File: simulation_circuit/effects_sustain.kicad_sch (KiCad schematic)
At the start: 14 parts, among them Q1 BC547

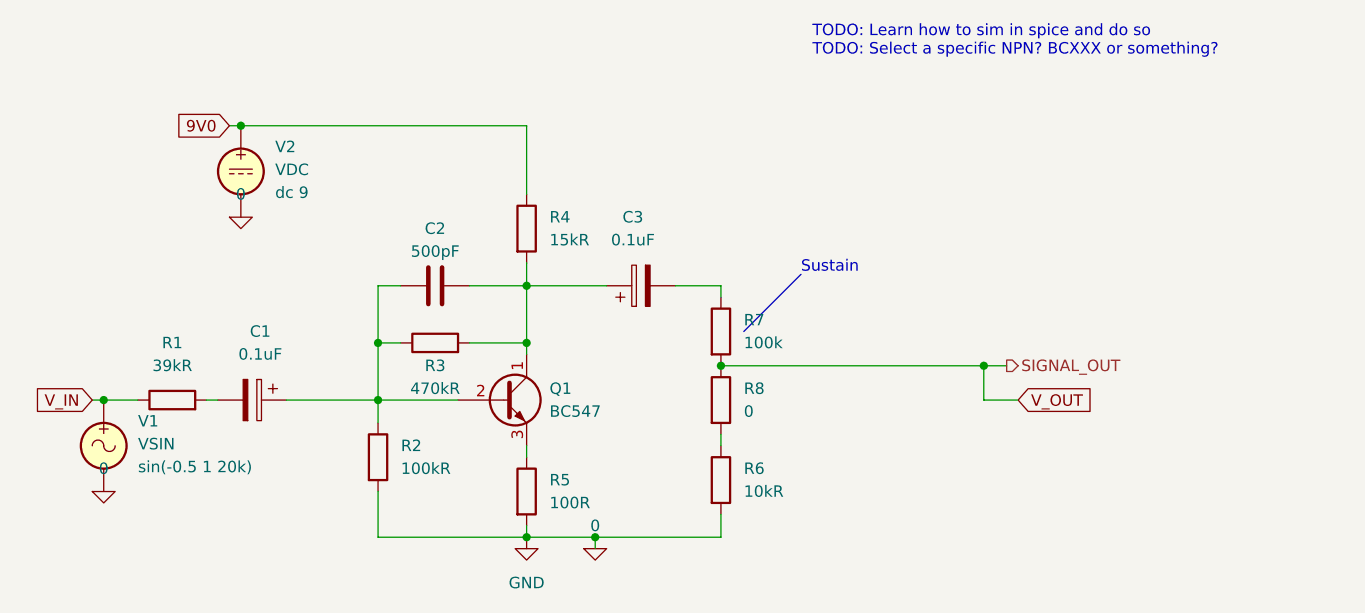
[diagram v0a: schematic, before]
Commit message: added decoupling cap and series resistor to output side of sustain effect, added subfolder to contain simulation results to put in design notes. Added simulation results for sustain effect to design notes
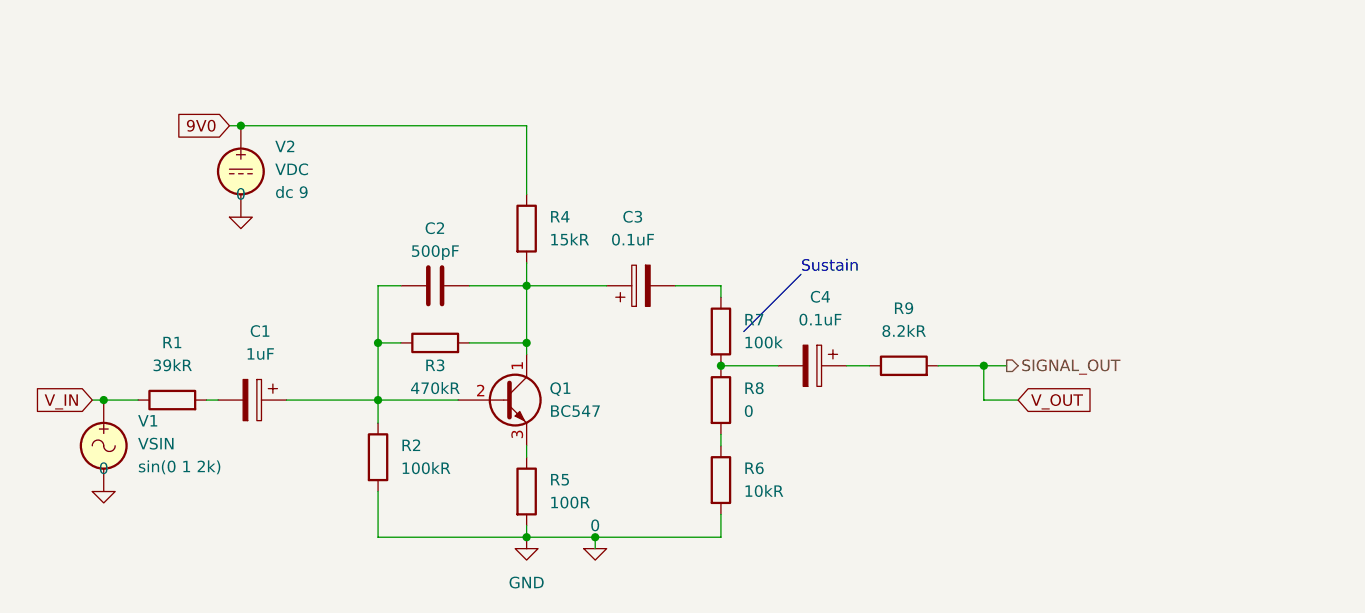
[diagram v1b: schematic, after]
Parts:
- added C4: 0.1uF, symbol Device:C_Polarized
- added R9: 8.2kR, symbol Device:R
- C1: value 0.1uF -> 1uF
- Q1: Spice_Lib_File /home/liam/Documents/big_muff_pi_copy/SPICE_MODELS.lib -> /home/liam/big_muff_pi_copy/SPICE_MODELS.lib
- V1: Spice_Model sin(-0.5 1 20k) -> sin(0 1 2k)
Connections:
- net V_OUT: now also R9.2; no longer R7.2, R8.1
- new net: C4.2, R7.2, R8.1
- new net: C4.1, R9.1
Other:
- note removed: "TODO: Learn how to sim in spice and do so TODO: Select a specific NPN? BCXXX or something?"
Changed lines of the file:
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@@
 (kicad_sch (version 20211123) (generator eeschema)
   (paper "A4")
+  (junction (at 148.59 109.22) (diameter 0) (color 0 0 0 0)
+  )
+  (junction (at 148.59 81.28) (diameter 0) (color 0 0 0 0)
+  )
+  (junction (at 116.84 63.5) (diameter 0) (color 0 0 0 0)
+  )
   (junction (at 170.18 90.17) (diameter 0) (color 0 0 0 0)
   )
-  (junction (at 148.59 109.22) (diameter 0) (color 0 0 0 0)
-  )
-  (junction (at 148.59 81.28) (diameter 0) (color 0 0 0 0)
-  )
-  (junction (at 116.84 63.5) (diameter 0) (color 0 0 0 0)
-  )
   (junction (at 132.08 93.98) (diameter 0) (color 0 0 0 0)
   )
@@
   )
   (wire (pts (xy 132.08 93.98) (xy 140.97 93.98))
-    (stroke (width 0) (type default) (color 0 0 0 0))
-  )
-  (wire (pts (xy 170.18 90.17) (xy 199.39 90.17))
     (stroke (width 0) (type default) (color 0 0 0 0))
   )
@@
     (stroke (width 0) (type default) (color 0 0 0 0))
   )
+  (wire (pts (xy 194.31 90.17) (xy 199.39 90.17))
+    (stroke (width 0) (type default) (color 0 0 0 0))
+  )
   (wire (pts (xy 148.59 107.95) (xy 148.59 109.22))
     (stroke (width 0) (type default) (color 0 0 0 0))
@@
     (stroke (width 0) (type default) (color 0 0 0 0))
   )
+  (wire (pts (xy 170.18 90.17) (xy 176.53 90.17))
+    (stroke (width 0) (type default) (color 0 0 0 0))
+  )
   (wire (pts (xy 199.39 90.17) (xy 201.93 90.17))
     (stroke (width 0) (type default) (color 0 0 0 0))
@@
     (stroke (width 0) (type default) (color 0 0 0 0))
   )
+  (wire (pts (xy 184.15 90.17) (xy 186.69 90.17))
+    (stroke (width 0) (type default) (color 0 0 0 0))
+  )
   (wire (pts (xy 148.59 78.74) (xy 148.59 81.28))
     (stroke (width 0) (type default) (color 0 0 0 0))
@@
   (wire (pts (xy 170.18 97.79) (xy 170.18 99.06))
     (stroke (width 0) (type default) (color 0 0 0 0))
-  )
-  (text "TODO: Learn how to sim in spice and do so\nTODO: Select a specific NPN? BCXXX or something?"
-    (at 180.34 55.88 0)
-    (effects (font (size 1.27 1.27)) (justify left bottom))
   )
   (text "Sustain" (at 179.07 80.01 0)
@@
     (pin "2")
   )
+  (symbol (lib_id "Device:C_Polarized") (at 180.34 90.17 270) (unit 1)
+    (in_bom yes) (on_board yes) (fields_autoplaced)
+    (property "Reference" "C4" (id 0) (at 181.229 82.55 90))
+    (property "Value" "0.1uF" (id 1) (at 181.229 85.09 90))
+    (property "Footprint" "" (id 2) (at 176.53 91.1352 0)
+      (effects (font (size 1.27 1.27)) hide)
+    )
+    (property "Datasheet" "~" (id 3) (at 180.34 90.17 0)
+      (effects (font (size 1.27 1.27)) hide)
+    )
+    (pin "1")
+    (pin "2")
+  )
   (symbol (lib_id "Simulation_SPICE:VDC") (at 116.84 68.58 0) (unit 1)
     (in_bom yes) (on_board yes) (fields_autoplaced)
@@
     (pin "2")
   )
+  (symbol (lib_id "Device:R") (at 190.5 90.17 90) (unit 1)
+    (in_bom yes) (on_board yes) (fields_autoplaced)
+    (property "Reference" "R9" (id 0) (at 190.5 83.82 90))
+    (property "Value" "8.2kR" (id 1) (at 190.5 86.36 90))
+    (property "Footprint" "" (id 2) (at 190.5 91.948 90)
+      (effects (font (size 1.27 1.27)) hide)
+    )
+    (property "Datasheet" "~" (id 3) (at 190.5 90.17 0)
+      (effects (font (size 1.27 1.27)) hide)
+    )
+    (pin "1")
+    (pin "2")
+  )
   (symbol (lib_id "Simulation_SPICE:VSIN") (at 101.6 99.06 0) (unit 1)
     (in_bom yes) (on_board yes) (fields_autoplaced)
@@
       (effects (font (size 1.27 1.27)) (justify left) hide)
     )
-    (property "Spice_Model" "sin(-0.5 1 20k)" (id 6) (at 105.41 101.4101 0)
+    (property "Spice_Model" "sin(0 1 2k)" (id 6) (at 105.41 101.4101 0)
       (effects (font (size 1.27 1.27)) (justify left))
     )
@@
     (in_bom yes) (on_board yes) (fields_autoplaced)
     (property "Reference" "C1" (id 0) (at 118.999 86.36 90))
-    (property "Value" "0.1uF" (id 1) (at 118.999 88.9 90))
+    (property "Value" "1uF" (id 1) (at 118.999 88.9 90))
     (property "Footprint" "" (id 2) (at 114.3 94.9452 0)
       (effects (font (size 1.27 1.27)) hide)
@@
       (effects (font (size 1.27 1.27)) hide)
     )
-    (property "Spice_Lib_File" "/home/liam/Documents/big_muff_pi_copy/SPICE_MODELS.lib" (id 7) (at 146.05 93.98 0)
-      (effects (font (size 1.27 1.27)) hide)
-    )
+    (property "Spice_Lib_File" "/home/liam/big_muff_pi_copy/SPICE_MODELS.lib" (id 7) (at 146.05 93.98 0)
+      (effects (font (size 1.27 1.27)) hide)
+    )
